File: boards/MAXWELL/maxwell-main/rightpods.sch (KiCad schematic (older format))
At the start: 3 parts

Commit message: Initial work on SERDES inputs
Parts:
- removed U?: XC7K160T-2FFG676C, symbol xilinx-azonenberg:XC7KxT-FFG676
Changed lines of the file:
@@
 $Descr A4 11693 8268
 encoding utf-8
-Sheet 9 14
+Sheet 9 15
 Title "MAXWELL Main Board"
 Date "2020-06-15"
@@
 AR Path="/5EDD71F2/5F2ECCDE" Ref="U?"  Part="9"
 AR Path="/5EDD723A/5F2ECCDE" Ref="U?"  Part="6"
+AR Path="/5EDD723A/5F2BB4CD/5F2ECCDE" Ref="U?"  Part="6"
 F 0 "U?" H 1850 5950 50  0000 L CNN
 F 1 "XC7K160T-2FFG676C" H 1850 5850 50  0000 L CNN
@@
 AR Path="/5EDD71F2/5F2ECCE4" Ref="U?"  Part="9"
 AR Path="/5EDD723A/5F2ECCE4" Ref="U?"  Part="8"
+AR Path="/5EDD723A/5F2BB4CD/5F2ECCE4" Ref="U?"  Part="8"
 F 0 "U?" H 3650 5950 50  0000 L CNN
 F 1 "XC7K160T-2FFG676C" H 3650 5850 50  0000 L CNN
@@
 	1    0    0    -1
 $EndComp
-$Comp
-L xilinx-azonenberg:XC7KxT-FFG676 U?
-U 13 1 5F2ECCEA
-P 5450 6000
-AR Path="/5EDD71F2/5F2ECCEA" Ref="U?"  Part="9"
-AR Path="/5EDD723A/5F2ECCEA" Ref="U?"  Part="13"
-F 0 "U?" H 5450 5950 50  0000 L CNN
-F 1 "XC7K160T-2FFG676C" H 5450 5850 50  0000 L CNN
-F 2 "" H 5450 6000 50  0001 C CNN
-F 3 "" H 5450 6000 50  0001 C CNN
-	13   5450 6000
-	1    0    0    -1
-$EndComp
+$Sheet
+S 8350 2300 1400 2600
+U 5F308105
+F0 "SERDES inputs" 50
+F1 "serdesinputs.sch" 50
+F2 "IN0_P" I L 8350 2350 50
+F3 "IN0_N" I L 8350 2450 50
+F4 "IN1_P" I L 8350 2650 50
+F5 "IN1_N" I L 8350 2750 50
+F6 "IN2_P" I L 8350 2950 50
+F7 "IN2_N" I L 8350 3050 50
+F8 "IN3_P" I L 8350 3250 50
+F9 "IN3_N" I L 8350 3350 50
+F10 "2V5" I R 9750 2350 50
+F11 "GND" I R 9750 2450 50
+F12 "MUX0_SEL" I R 9750 2650 50
+F13 "EXT_TRIG_P" I L 8350 3550 50
+F14 "EXT_TRIG_N" I L 8350 3650 50
+F15 "MUX0_EQ" I R 9750 2750 50
+F16 "REFCLK_P" I L 8350 3850 50
+F17 "REFCLK_N" I L 8350 3950 50
+F18 "MUX1_SEL" I R 9750 2950 50
+F19 "MUX1_EQ" I R 9750 3050 50
+F20 "SYNC_CLK_P" I L 8350 4150 50
+F21 "SYNC_CLK_N" I L 8350 4250 50
+F22 "MUX2_SEL" I R 9750 3250 50
+F23 "MUX3_SEL" I R 9750 3550 50
+F24 "MUX3_EQ" I R 9750 3650 50
+F25 "MUX2_EQ" I R 9750 3350 50
+$EndSheet
 $EndSCHEMATC

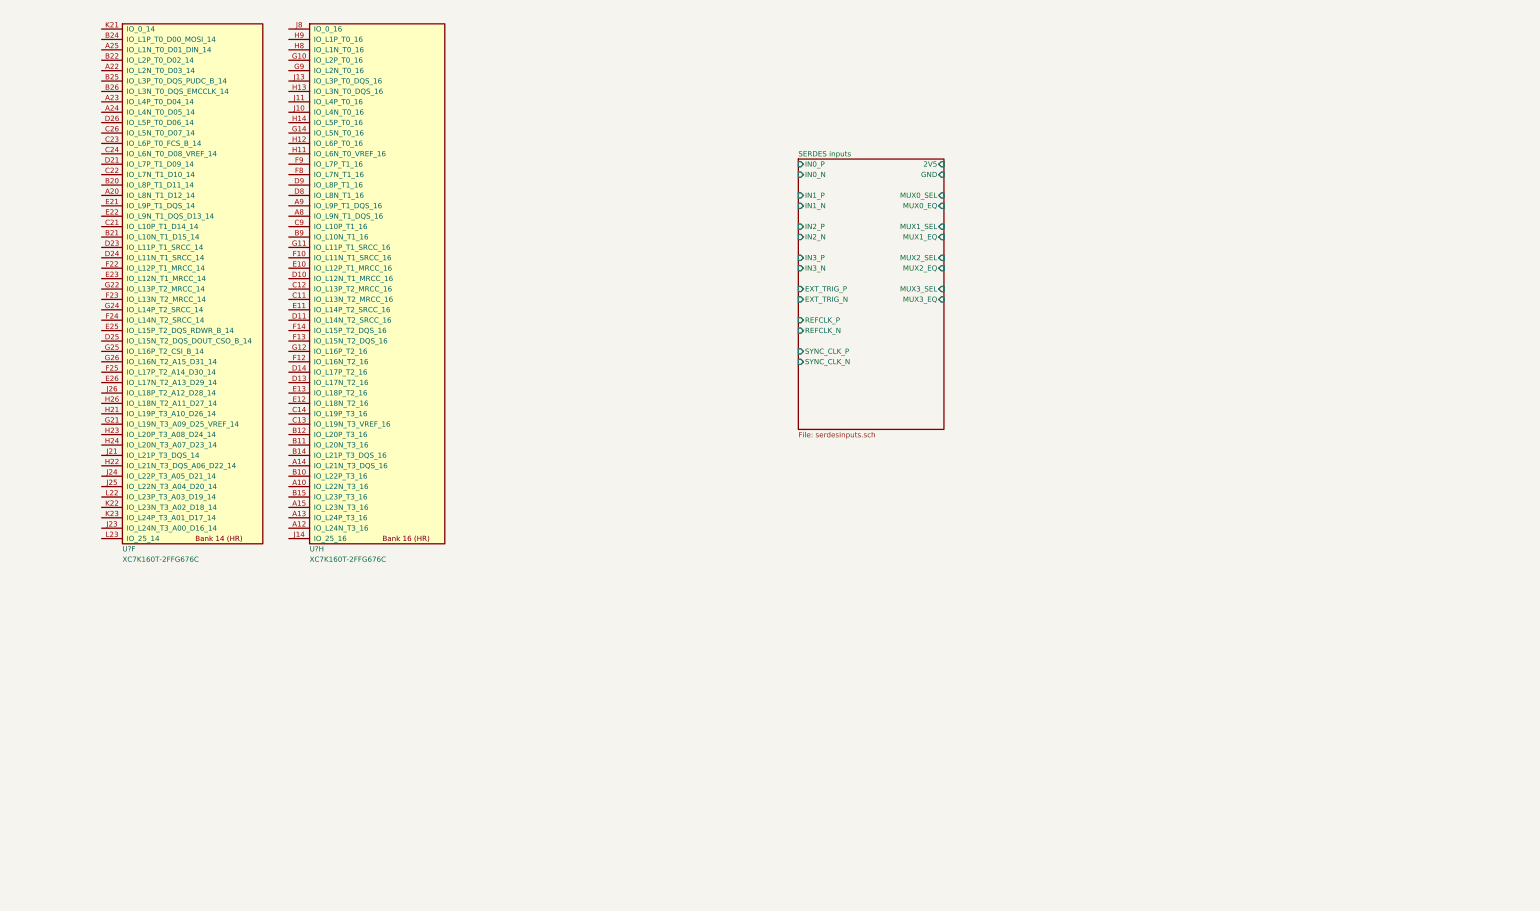
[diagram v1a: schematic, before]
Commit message: Schematic for right side inputs
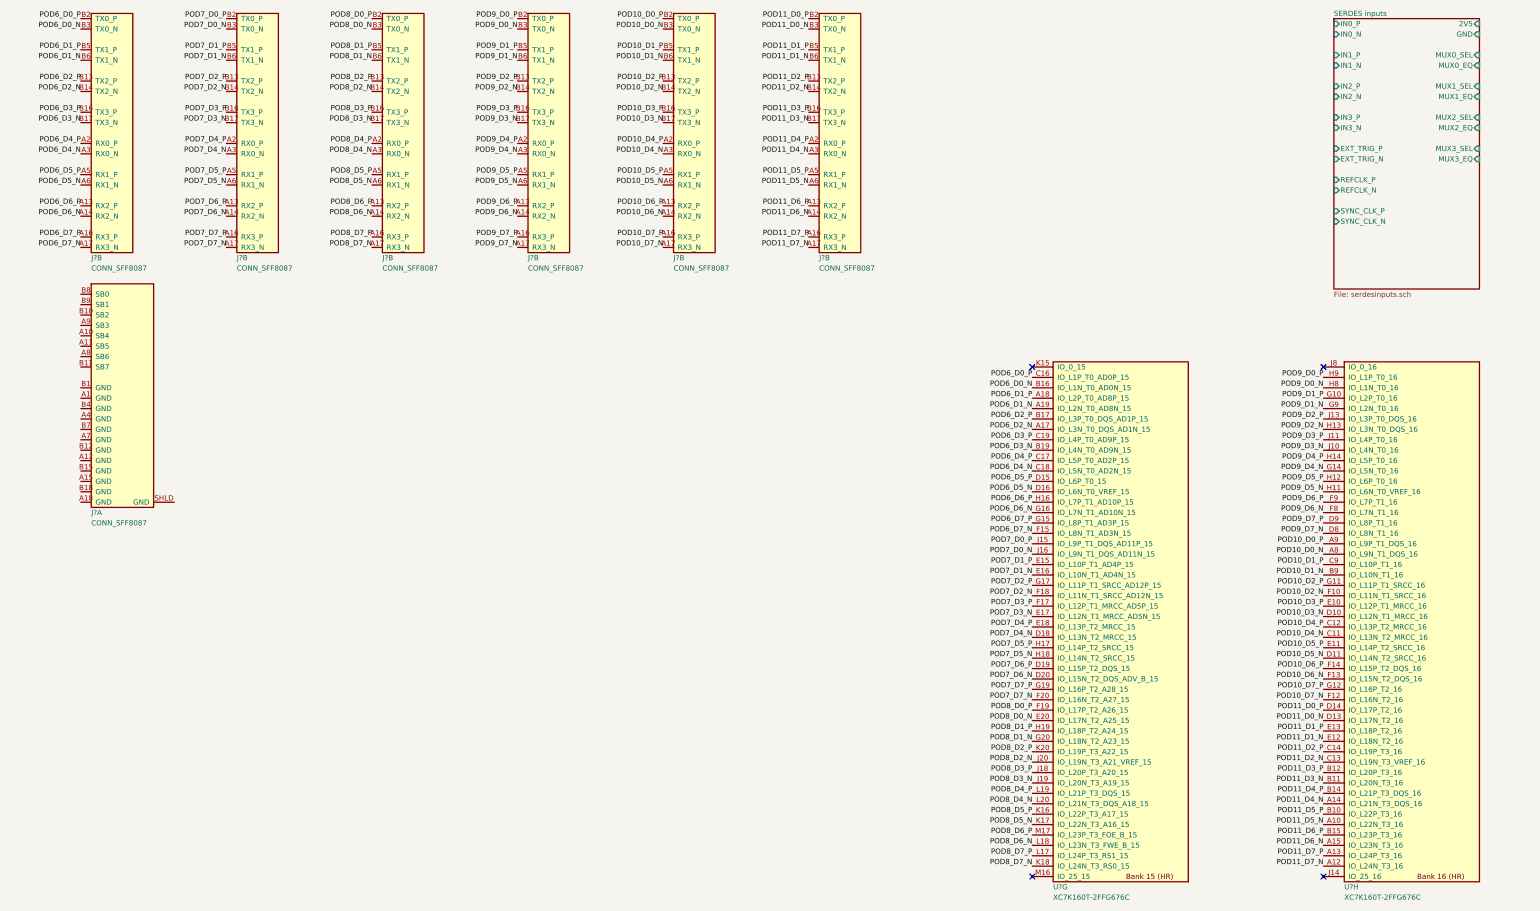
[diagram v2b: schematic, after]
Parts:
- added J? (x7): CONN_SFF8087, symbol special-azonenberg:CONN_SFF8087
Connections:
- net POD11_D5_N: now reaches U?.A10 (IO_L22N_T3_16)
- net POD11_D5_N: now also J?.A6 (RX1_N)
- net POD11_D7_N: now reaches U?.A12 (IO_L24N_T3_16)
- net POD11_D7_N: now also J?.A17 (RX3_N)
- net POD11_D7_P: now reaches U?.A13 (IO_L24P_T3_16)
- net POD11_D7_P: now also J?.A16 (RX3_P)
- net POD11_D4_N: now reaches U?.A14 (IO_L21N_T3_DQS_16)
- net POD11_D4_N: now also J?.A3 (RX0_N)
- net POD11_D6_N: now reaches U?.A15 (IO_L23N_T3_16)
- net POD11_D6_N: now also J?.A14 (RX2_N)
- net POD10_D0_N: now reaches U?.A8 (IO_L9N_T1_DQS_16)
- net POD10_D0_N: now also J?.B3 (TX0_N)
- net POD10_D0_P: now reaches U?.A9 (IO_L9P_T1_DQS_16)
- net POD10_D0_P: now also J?.B2 (TX0_P)
- net POD11_D5_P: now reaches U?.B10 (IO_L22P_T3_16)
- net POD11_D5_P: now also J?.A5 (RX1_P)
- net POD11_D3_N: now reaches U?.B11 (IO_L20N_T3_16)
- net POD11_D3_N: now also J?.B17 (TX3_N)
- net POD11_D3_P: now reaches U?.B12 (IO_L20P_T3_16)
- net POD11_D3_P: now also J?.B16 (TX3_P)
- net POD11_D4_P: now reaches U?.B14 (IO_L21P_T3_DQS_16)
- net POD11_D4_P: now also J?.A2 (RX0_P)
- net POD11_D6_P: now reaches U?.B15 (IO_L23P_T3_16)
- net POD11_D6_P: now also J?.A13 (RX2_P)
- net POD10_D1_N: now reaches U?.B9 (IO_L10N_T1_16)
- net POD10_D1_N: now also J?.B6 (TX1_N)
- net POD10_D4_N: now reaches U?.C11 (IO_L13N_T2_MRCC_16)
- net POD10_D4_N: now also J?.A3 (RX0_N)
- net POD10_D4_P: now reaches U?.C12 (IO_L13P_T2_MRCC_16)
- net POD10_D4_P: now also J?.A2 (RX0_P)
- net POD11_D2_N: now reaches U?.C13 (IO_L19N_T3_VREF_16)
- net POD11_D2_N: now also J?.B14 (TX2_N)
- net POD11_D2_P: now reaches U?.C14 (IO_L19P_T3_16)
- net POD11_D2_P: now also J?.B13 (TX2_P)
- net POD10_D1_P: now reaches U?.C9 (IO_L10P_T1_16)
- net POD10_D1_P: now also J?.B5 (TX1_P)
- net POD10_D3_N: now reaches U?.D10 (IO_L12N_T1_MRCC_16)
- net POD10_D3_N: now also J?.B17 (TX3_N)
- net POD10_D5_N: now reaches U?.D11 (IO_L14N_T2_SRCC_16)
- net POD10_D5_N: now also J?.A6 (RX1_N)
- net POD11_D0_N: now reaches U?.D13 (IO_L17N_T2_16)
- net POD11_D0_N: now also J?.B3 (TX0_N)
- net POD11_D0_P: now reaches U?.D14 (IO_L17P_T2_16)
- net POD11_D0_P: now also J?.B2 (TX0_P)
- net POD9_D7_N: now reaches U?.D8 (IO_L8N_T1_16)
- net POD9_D7_N: now also J?.A17 (RX3_N)
- net POD9_D7_P: now reaches U?.D9 (IO_L8P_T1_16)
- net POD9_D7_P: now also J?.A16 (RX3_P)
- net POD10_D3_P: now reaches U?.E10 (IO_L12P_T1_MRCC_16)
- net POD10_D3_P: now also J?.B16 (TX3_P)
- net POD10_D5_P: now reaches U?.E11 (IO_L14P_T2_SRCC_16)
- net POD10_D5_P: now also J?.A5 (RX1_P)
- net POD11_D1_N: now reaches U?.E12 (IO_L18N_T2_16)
- net POD11_D1_N: now also J?.B6 (TX1_N)
- net POD11_D1_P: now reaches U?.E13 (IO_L18P_T2_16)
- net POD11_D1_P: now also J?.B5 (TX1_P)
- net POD10_D2_N: now reaches U?.F10 (IO_L11N_T1_SRCC_16)
- net POD10_D2_N: now also J?.B14 (TX2_N)
- net POD10_D7_N: now reaches U?.F12 (IO_L16N_T2_16)
- net POD10_D7_N: now also J?.A17 (RX3_N)
- net POD10_D6_N: now reaches U?.F13 (IO_L15N_T2_DQS_16)
- net POD10_D6_N: now also J?.A14 (RX2_N)
- net POD10_D6_P: now reaches U?.F14 (IO_L15P_T2_DQS_16)
- net POD10_D6_P: now also J?.A13 (RX2_P)
- net POD9_D6_N: now reaches U?.F8 (IO_L7N_T1_16)
- net POD9_D6_N: now also J?.A14 (RX2_N)
- net POD9_D6_P: now reaches U?.F9 (IO_L7P_T1_16)
- net POD9_D6_P: now also J?.A13 (RX2_P)
- net POD9_D1_P: now reaches U?.G10 (IO_L2P_T0_16)
- net POD9_D1_P: now also J?.B5 (TX1_P)
- net POD10_D2_P: now reaches U?.G11 (IO_L11P_T1_SRCC_16)
- net POD10_D2_P: now also J?.B13 (TX2_P)
- net POD10_D7_P: now reaches U?.G12 (IO_L16P_T2_16)
- net POD10_D7_P: now also J?.A16 (RX3_P)
- net POD9_D4_N: now reaches U?.G14 (IO_L5N_T0_16)
- net POD9_D4_N: now also J?.A3 (RX0_N)
- net POD9_D1_N: now reaches U?.G9 (IO_L2N_T0_16)
- net POD9_D1_N: now also J?.B6 (TX1_N)
- net POD9_D5_N: now reaches U?.H11 (IO_L6N_T0_VREF_16)
- net POD9_D5_N: now also J?.A6 (RX1_N)
- net POD9_D5_P: now reaches U?.H12 (IO_L6P_T0_16)
- net POD9_D5_P: now also J?.A5 (RX1_P)
- net POD9_D2_N: now reaches U?.H13 (IO_L3N_T0_DQS_16)
- net POD9_D2_N: now also J?.B14 (TX2_N)
- net POD9_D4_P: now reaches U?.H14 (IO_L5P_T0_16)
- net POD9_D4_P: now also J?.A2 (RX0_P)
- net POD9_D0_N: now reaches U?.H8 (IO_L1N_T0_16)
- net POD9_D0_N: now also J?.B3 (TX0_N)
- net POD9_D0_P: now reaches U?.H9 (IO_L1P_T0_16)
- net POD9_D0_P: now also J?.B2 (TX0_P)
- net POD9_D3_N: now reaches U?.J10 (IO_L4N_T0_16)
- net POD9_D3_N: now also J?.B17 (TX3_N)
- net POD9_D3_P: now reaches U?.J11 (IO_L4P_T0_16)
- net POD9_D3_P: now also J?.B16 (TX3_P)
- net POD9_D2_P: now reaches U?.J13 (IO_L3P_T0_DQS_16)
- net POD9_D2_P: now also J?.B13 (TX2_P)
- new net POD6_D0_N: J?.B3 (TX0_N), U?.B16 (IO_L1N_T0_AD0N_15)
- new net POD6_D0_P: J?.B2 (TX0_P), U?.C16 (IO_L1P_T0_AD0P_15)
- new net POD6_D1_N: J?.B6 (TX1_N), U?.A19 (IO_L2N_T0_AD8N_15)
- new net POD6_D1_P: J?.B5 (TX1_P), U?.A18 (IO_L2P_T0_AD8P_15)
- new net POD6_D2_N: J?.B14 (TX2_N), U?.A17 (IO_L3N_T0_DQS_AD1N_15)
- new net POD6_D2_P: J?.B13 (TX2_P), U?.B17 (IO_L3P_T0_DQS_AD1P_15)
- new net POD6_D3_N: J?.B17 (TX3_N), U?.B19 (IO_L4N_T0_AD9N_15)
- new net POD6_D3_P: J?.B16 (TX3_P), U?.C19 (IO_L4P_T0_AD9P_15)
- new net POD6_D4_N: J?.A3 (RX0_N), U?.C18 (IO_L5N_T0_AD2N_15)
- new net POD6_D4_P: J?.A2 (RX0_P), U?.C17 (IO_L5P_T0_AD2P_15)
- new net POD6_D5_N: J?.A6 (RX1_N), U?.D16 (IO_L6N_T0_VREF_15)
- new net POD6_D5_P: J?.A5 (RX1_P), U?.D15 (IO_L6P_T0_15)
- new net POD6_D6_N: J?.A14 (RX2_N), U?.G16 (IO_L7N_T1_AD10N_15)
- new net POD6_D6_P: J?.A13 (RX2_P), U?.H16 (IO_L7P_T1_AD10P_15)
- new net POD6_D7_N: J?.A17 (RX3_N), U?.F15 (IO_L8N_T1_AD3N_15)
- new net POD6_D7_P: J?.A16 (RX3_P), U?.G15 (IO_L8P_T1_AD3P_15)
- new net POD7_D0_N: J?.B3 (TX0_N), U?.J16 (IO_L9N_T1_DQS_AD11N_15)
- new net POD7_D0_P: J?.B2 (TX0_P), U?.J15 (IO_L9P_T1_DQS_AD11P_15)
- new net POD7_D1_N: J?.B6 (TX1_N), U?.E16 (IO_L10N_T1_AD4N_15)
- new net POD7_D1_P: J?.B5 (TX1_P), U?.E15 (IO_L10P_T1_AD4P_15)
- new net POD7_D2_N: J?.B14 (TX2_N), U?.F18 (IO_L11N_T1_SRCC_AD12N_15)
- new net POD7_D2_P: J?.B13 (TX2_P), U?.G17 (IO_L11P_T1_SRCC_AD12P_15)
- new net POD7_D3_N: J?.B17 (TX3_N), U?.E17 (IO_L12N_T1_MRCC_AD5N_15)
- new net POD7_D3_P: J?.B16 (TX3_P), U?.F17 (IO_L12P_T1_MRCC_AD5P_15)
- new net POD7_D4_N: J?.A3 (RX0_N), U?.D18 (IO_L13N_T2_MRCC_15)
- new net POD7_D4_P: J?.A2 (RX0_P), U?.E18 (IO_L13P_T2_MRCC_15)
- new net POD7_D5_N: J?.A6 (RX1_N), U?.H18 (IO_L14N_T2_SRCC_15)
- new net POD7_D5_P: J?.A5 (RX1_P), U?.H17 (IO_L14P_T2_SRCC_15)
- new net POD7_D6_N: J?.A14 (RX2_N), U?.D20 (IO_L15N_T2_DQS_ADV_B_15)
- new net POD7_D6_P: J?.A13 (RX2_P), U?.D19 (IO_L15P_T2_DQS_15)
- new net POD7_D7_N: J?.A17 (RX3_N), U?.F20 (IO_L16N_T2_A27_15)
- new net POD7_D7_P: J?.A16 (RX3_P), U?.G19 (IO_L16P_T2_A28_15)
- new net POD8_D0_N: J?.B3 (TX0_N), U?.E20 (IO_L17N_T2_A25_15)
- new net POD8_D0_P: J?.B2 (TX0_P), U?.F19 (IO_L17P_T2_A26_15)
- new net POD8_D1_N: J?.B6 (TX1_N), U?.G20 (IO_L18N_T2_A23_15)
- new net POD8_D1_P: J?.B5 (TX1_P), U?.H19 (IO_L18P_T2_A24_15)
- new net POD8_D2_N: J?.B14 (TX2_N), U?.J20 (IO_L19N_T3_A21_VREF_15)
- new net POD8_D2_P: J?.B13 (TX2_P), U?.K20 (IO_L19P_T3_A22_15)
- new net POD8_D3_N: J?.B17 (TX3_N), U?.J19 (IO_L20N_T3_A19_15)
- new net POD8_D3_P: J?.B16 (TX3_P), U?.J18 (IO_L20P_T3_A20_15)
- new net POD8_D4_N: J?.A3 (RX0_N), U?.L20 (IO_L21N_T3_DQS_A18_15)
- new net POD8_D4_P: J?.A2 (RX0_P), U?.L19 (IO_L21P_T3_DQS_15)
- new net POD8_D5_N: J?.A6 (RX1_N), U?.K17 (IO_L22N_T3_A16_15)
- new net POD8_D5_P: J?.A5 (RX1_P), U?.K16 (IO_L22P_T3_A17_15)
- new net POD8_D6_N: J?.A14 (RX2_N), U?.L18 (IO_L23N_T3_FWE_B_15)
- new net POD8_D6_P: J?.A13 (RX2_P), U?.M17 (IO_L23P_T3_FOE_B_15)
- new net POD8_D7_N: J?.A17 (RX3_N), U?.K18 (IO_L24N_T3_RS0_15)
- new net POD8_D7_P: J?.A16 (RX3_P), U?.L17 (IO_L24P_T3_RS1_15)
- no-connect marks 0 -> 4
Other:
- moved on the sheet: U?H

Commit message: Continued work on right side pods
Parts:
- added J? (x5): CONN_SFF8087, symbol special-azonenberg:CONN_SFF8087
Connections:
- net POD10_D3_N: now also U?.C11 (IO_L13N_T2_MRCC_16); no longer U?.D10 (IO_L12N_T1_MRCC_16)
- net POD10_D4_N: now also U?.D11 (IO_L14N_T2_SRCC_16); no longer U?.C11 (IO_L13N_T2_MRCC_16)
- net POD10_D4_P: now also U?.E11 (IO_L14P_T2_SRCC_16); no longer U?.C12 (IO_L13P_T2_MRCC_16)
- net POD10_D5_N: now also U?.F13 (IO_L15N_T2_DQS_16); no longer U?.D11 (IO_L14N_T2_SRCC_16)
- net POD10_D5_P: now also U?.F14 (IO_L15P_T2_DQS_16); no longer U?.E11 (IO_L14P_T2_SRCC_16)
- net POD10_D6_N: now also U?.F12 (IO_L16N_T2_16); no longer U?.F13 (IO_L15N_T2_DQS_16)
- net POD10_D6_P: now also U?.G12 (IO_L16P_T2_16); no longer U?.F14 (IO_L15P_T2_DQS_16)
- net POD10_D7_N: now also U?.D13 (IO_L17N_T2_16); no longer U?.F12 (IO_L16N_T2_16)
- net POD10_D7_P: now also U?.D14 (IO_L17P_T2_16); no longer U?.G12 (IO_L16P_T2_16)
- net POD11_D0_N: now also U?.E12 (IO_L18N_T2_16); no longer U?.D13 (IO_L17N_T2_16)
- net POD11_D0_P: now also U?.E13 (IO_L18P_T2_16); no longer U?.D14 (IO_L17P_T2_16)
- net POD11_D1_N: now also U?.C13 (IO_L19N_T3_VREF_16); no longer U?.E12 (IO_L18N_T2_16)
- net POD11_D1_P: now also U?.C14 (IO_L19P_T3_16); no longer U?.E13 (IO_L18P_T2_16)
- net POD11_D2_N: now also U?.B11 (IO_L20N_T3_16); no longer U?.C13 (IO_L19N_T3_VREF_16)
- net POD11_D2_P: now also U?.B12 (IO_L20P_T3_16); no longer U?.C14 (IO_L19P_T3_16)
- net POD11_D3_N: now also U?.A14 (IO_L21N_T3_DQS_16); no longer U?.B11 (IO_L20N_T3_16)
- net POD11_D3_P: now also U?.B14 (IO_L21P_T3_DQS_16); no longer U?.B12 (IO_L20P_T3_16)
- net POD11_D4_N: no longer U?.A14 (IO_L21N_T3_DQS_16)
- net POD11_D4_P: no longer U?.B14 (IO_L21P_T3_DQS_16)
- net POD11_D5_N: no longer U?.A10 (IO_L22N_T3_16)
- net POD11_D5_P: no longer U?.B10 (IO_L22P_T3_16)
- net POD11_D6_N: no longer U?.A15 (IO_L23N_T3_16)
- net POD11_D6_P: no longer U?.B15 (IO_L23P_T3_16)
- net POD11_D7_N: no longer U?.A12 (IO_L24N_T3_16)
- net POD11_D7_P: no longer U?.A13 (IO_L24P_T3_16)
- net GND: now reaches J?.A1 (GND)
- net GND: now also J?.A12 (GND), J?.A15 (GND), J?.A18 (GND), J?.A4 (GND), J?.A7 (GND), J?.B1 (GND), J?.B12 (GND), J?.B15 (GND), J?.B18 (GND), J?.B4 (GND), J?.B7 (GND)
- new net K7_CLK_N: U?.C12 (IO_L13P_T2_MRCC_16)
- new net K7_CLK_P: U?.D10 (IO_L12N_T1_MRCC_16)
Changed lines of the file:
@@
 Text Label 8450 3150 2    50   ~ 0
 POD11_D7_N
-Text Label 13400 7000 2    50   ~ 0
+Text Label 13400 7200 2    50   ~ 0
 POD10_D5_P
-Text Label 13400 7100 2    50   ~ 0
+Text Label 13400 7300 2    50   ~ 0
 POD10_D5_N
-Text Label 13400 7200 2    50   ~ 0
+Text Label 13400 7400 2    50   ~ 0
 POD10_D6_P
-Text Label 13400 7300 2    50   ~ 0
+Text Label 13400 7500 2    50   ~ 0
 POD10_D6_N
-Text Label 13400 7400 2    50   ~ 0
+Text Label 13400 7600 2    50   ~ 0
 POD10_D7_P
-Text Label 13400 7500 2    50   ~ 0
+Text Label 13400 7700 2    50   ~ 0
 POD10_D7_N
-Text Label 13400 7600 2    50   ~ 0
+Text Label 13400 7800 2    50   ~ 0
 POD11_D0_P
-Text Label 13400 7700 2    50   ~ 0
+Text Label 13400 7900 2    50   ~ 0
 POD11_D0_N
-Text Label 13400 7800 2    50   ~ 0
+Text Label 13400 8000 2    50   ~ 0
 POD11_D1_P
-Text Label 13400 7900 2    50   ~ 0
+Text Label 13400 8100 2    50   ~ 0
 POD11_D1_N
+Text Label 13400 8400 2    50   ~ 0
+POD11_D3_P
+Text Label 13400 8500 2    50   ~ 0
+POD11_D3_N
 Text Label 13400 8200 2    50   ~ 0
-POD11_D3_P
+POD11_D2_P
 Text Label 13400 8300 2    50   ~ 0
-POD11_D3_N
-Text Label 13400 8000 2    50   ~ 0
-POD11_D2_P
-Text Label 13400 8100 2    50   ~ 0
 POD11_D2_N
-Text Label 13400 8400 2    50   ~ 0
+Text Label 12400 1650 2    50   ~ 0
 POD11_D4_P
-Text Label 13400 8500 2    50   ~ 0
+Text Label 12400 1750 2    50   ~ 0
 POD11_D4_N
-Text Label 13400 8600 2    50   ~ 0
+Text Label 12400 1850 2    50   ~ 0
 POD11_D5_P
-Text Label 13400 8700 2    50   ~ 0
+Text Label 12400 1950 2    50   ~ 0
 POD11_D5_N
-Text Label 13400 8800 2    50   ~ 0
+Text Label 12400 2050 2    50   ~ 0
 POD11_D6_P
-Text Label 13400 8900 2    50   ~ 0
+Text Label 12400 2150 2    50   ~ 0
 POD11_D6_N
-Text Label 13400 9000 2    50   ~ 0
+Text Label 12400 2250 2    50   ~ 0
 POD11_D7_P
-Text Label 13400 9100 2    50   ~ 0
+Text Label 12400 2350 2    50   ~ 0
 POD11_D7_N
 Text Label 10600 4900 2    50   ~ 0
@@
 Text Label 10600 4400 2    50   ~ 0
 POD6_D0_P
-Text Label 13400 6900 2    50   ~ 0
+Text Label 13400 7100 2    50   ~ 0
 POD10_D4_N
-Text Label 13400 6800 2    50   ~ 0
+Text Label 13400 7000 2    50   ~ 0
 POD10_D4_P
 Text Label 13400 6500 2    50   ~ 0
@@
 Text Label 13400 6400 2    50   ~ 0
 POD10_D2_P
-Text Label 13400 6700 2    50   ~ 0
+Text Label 13400 6900 2    50   ~ 0
 POD10_D3_N
 Text Label 13400 6600 2    50   ~ 0
@@
 NoConn ~ 10600 4300
 NoConn ~ 10600 9200
+Text HLabel 13400 6700 0    50   Input ~ 0
+K7_CLK_P
+Text HLabel 13400 6800 0    50   Input ~ 0
+K7_CLK_N
+$Comp
+L special-azonenberg:CONN_SFF8087 J?
+U 1 1 5F4F0590
+P 2950 5650
+F 0 "J?" H 2950 5600 50  0000 L CNN
+F 1 "CONN_SFF8087" H 2950 5500 50  0000 L CNN
+F 2 "" H 2950 5650 50  0001 C CNN
+F 3 "" H 2950 5650 50  0001 C CNN
+	1    2950 5650
+	1    0    0    -1
+$EndComp
+$Comp
+L special-azonenberg:CONN_SFF8087 J?
+U 1 1 5F4F181F
+P 4350 5650
+F 0 "J?" H 4350 5600 50  0000 L CNN
+F 1 "CONN_SFF8087" H 4350 5500 50  0000 L CNN
+F 2 "" H 4350 5650 50  0001 C CNN
+F 3 "" H 4350 5650 50  0001 C CNN
+	1    4350 5650
+	1    0    0    -1
+$EndComp
+$Comp
+L special-azonenberg:CONN_SFF8087 J?
+U 1 1 5F4F28DA
+P 5750 5650
+F 0 "J?" H 5750 5600 50  0000 L CNN
+F 1 "CONN_SFF8087" H 5750 5500 50  0000 L CNN
+F 2 "" H 5750 5650 50  0001 C CNN
+F 3 "" H 5750 5650 50  0001 C CNN
+	1    5750 5650
+	1    0    0    -1
+$EndComp
+$Comp
+L special-azonenberg:CONN_SFF8087 J?
+U 1 1 5F4F3578
+P 7150 5650
+F 0 "J?" H 7150 5600 50  0000 L CNN
+F 1 "CONN_SFF8087" H 7150 5500 50  0000 L CNN
+F 2 "" H 7150 5650 50  0001 C CNN
+F 3 "" H 7150 5650 50  0001 C CNN
+	1    7150 5650
+	1    0    0    -1
+$EndComp
+$Comp
+L special-azonenberg:CONN_SFF8087 J?
+U 1 1 5F4F4453
+P 8550 5650
+F 0 "J?" H 8550 5600 50  0000 L CNN
+F 1 "CONN_SFF8087" H 8550 5500 50  0000 L CNN
+F 2 "" H 8550 5650 50  0001 C CNN
+F 3 "" H 8550 5650 50  0001 C CNN
+	1    8550 5650
+	1    0    0    -1
+$EndComp
+Text HLabel 1550 6200 0    50   Output ~ 0
+POD6_UART_TX
+Text HLabel 1550 6300 0    50   Input ~ 0
+POD6_UART_RX
+Text HLabel 1550 6500 0    50   Output ~ 0
+POD7_UART_TX
+Text HLabel 1550 6600 0    50   Input ~ 0
+POD7_UART_RX
+Text HLabel 1550 6800 0    50   Output ~ 0
+POD8_UART_TX
+Text HLabel 1550 6900 0    50   Input ~ 0
+POD8_UART_RX
+Text HLabel 1550 7100 0    50   Output ~ 0
+POD9_UART_TX
+Text HLabel 1550 7200 0    50   Input ~ 0
+POD9_UART_RX
+Text HLabel 1550 7400 0    50   Output ~ 0
+POD10_UART_TX
+Text HLabel 1550 7500 0    50   Input ~ 0
+POD10_UART_RX
+Text HLabel 1550 7700 0    50   Output ~ 0
+POD11_UART_TX
+Text HLabel 1550 7800 0    50   Input ~ 0
+POD11_UART_RX
+Text Label 1450 4500 2    50   ~ 0
+GND
+Wire Wire Line
+	1450 4500 1450 4600
+Connection ~ 1450 4600
+Wire Wire Line
+	1450 4600 1450 4700
+Connection ~ 1450 4700
+Wire Wire Line
+	1450 4700 1450 4800
+Connection ~ 1450 4800
+Wire Wire Line
+	1450 4800 1450 4900
+Connection ~ 1450 4900
+Wire Wire Line
+	1450 4900 1450 5000
+Connection ~ 1450 5000
+Wire Wire Line
+	1450 5000 1450 5100
+Connection ~ 1450 5100
+Wire Wire Line
+	1450 5100 1450 5200
+Connection ~ 1450 5200
+Wire Wire Line
+	1450 5200 1450 5300
+Connection ~ 1450 5300
+Wire Wire Line
+	1450 5300 1450 5400
+Connection ~ 1450 5400
+Wire Wire Line
+	1450 5400 1450 5500
+Connection ~ 1450 5500
+Wire Wire Line
+	1450 5500 1450 5600
 $EndSCHEMATC
